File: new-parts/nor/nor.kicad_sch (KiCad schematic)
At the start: 35 parts, among them J1 BHR-10-VUA, J2 BHR-10-VUA, J3 BHR-10-VUA, K1 J104D2C12VDC.15S, K2 J104D2C12VDC.15S, K3 J104D2C12VDC.15S, K4 J104D2C12VDC.15S, K5 J104D2C12VDC.15S, K6 J104D2C12VDC.15S, K7 J104D2C12VDC.15S, K8 J104D2C12VDC.15S

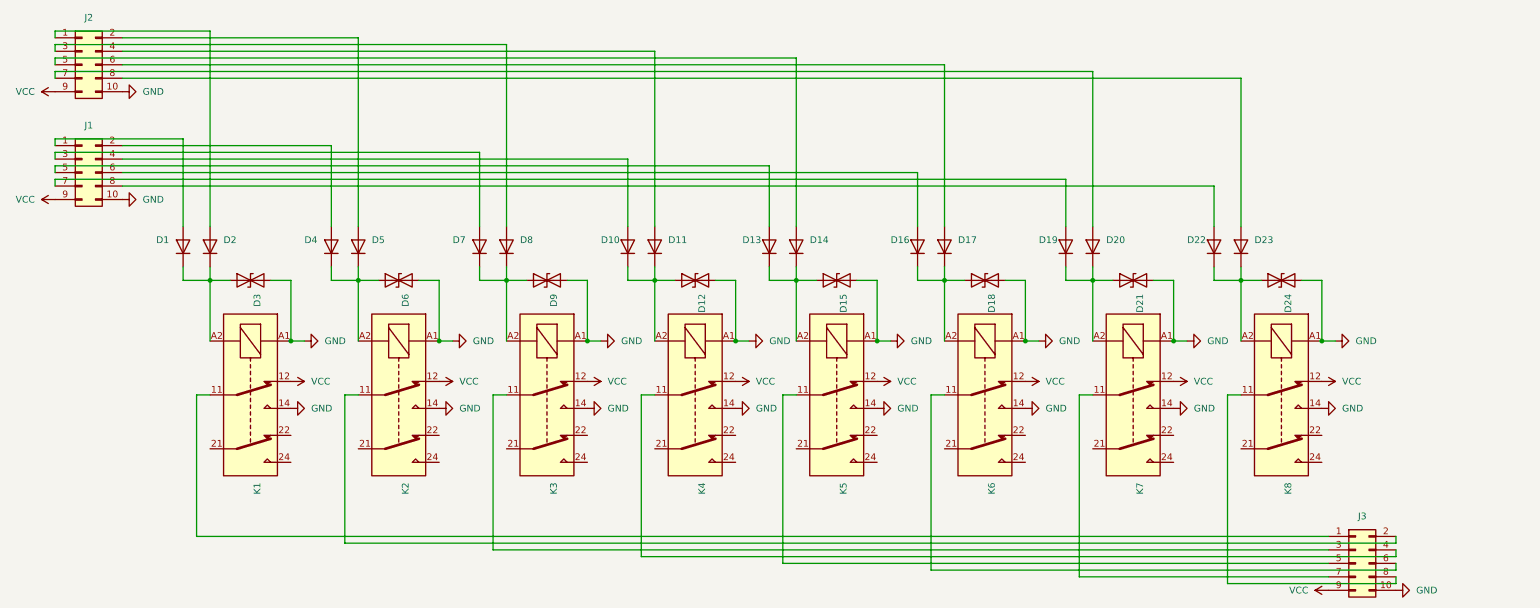
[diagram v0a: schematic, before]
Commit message: Perform BOM export (changes some project settings).
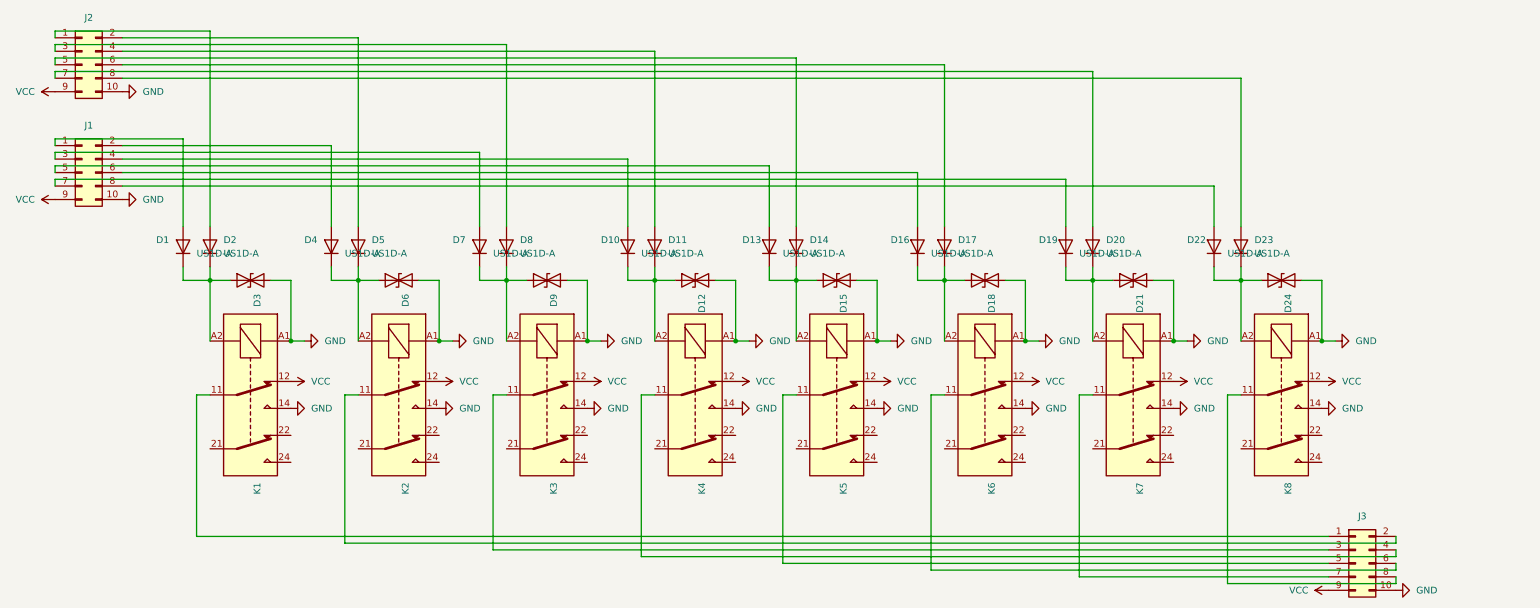
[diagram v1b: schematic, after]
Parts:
- D1, D10, D11, D13, D14, D16, D17, D19, D2, D20, D22, D23, D4, D5, D7, D8: value ~ -> US1D-A
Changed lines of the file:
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@@
 			)
 		)
-		(property "Value" "~"
+		(property "Value" "US1D-A"
 			(at 191.77 69.85 90)
 			(effects
@@
 			)
 		)
-		(property "Datasheet" "~"
+		(property "Datasheet" "https://mm.digikey.com/Volume0/opasdata/d220001/medias/docus/5561/US1A-A%20thru%20US1M-A.pdf"
 			(at 189.23 68.58 0)
 			(effects
@@
 			)
 		)
-		(property "Value" "~"
+		(property "Value" "US1D-A"
 			(at 168.91 69.85 90)
 			(effects
@@
 			)
 		)
-		(property "Datasheet" "~"
+		(property "Datasheet" "https://mm.digikey.com/Volume0/opasdata/d220001/medias/docus/5561/US1A-A%20thru%20US1M-A.pdf"
 			(at 166.37 68.58 0)
 			(effects
@@
 			)
 		)
-		(property "Value" "~"
+		(property "Value" "US1D-A"
 			(at 252.73 69.85 90)
 			(effects
@@
 			)
 		)
-		(property "Datasheet" "~"
+		(property "Datasheet" "https://mm.digikey.com/Volume0/opasdata/d220001/medias/docus/5561/US1A-A%20thru%20US1M-A.pdf"
 			(at 250.19 68.58 0)
 			(effects
@@
 			)
 		)
-		(property "Value" "~"
+		(property "Value" "US1D-A"
 			(at 247.65 69.85 90)
 			(effects
@@
 			)
 		)
-		(property "Datasheet" "~"
+		(property "Datasheet" "https://mm.digikey.com/Volume0/opasdata/d220001/medias/docus/5561/US1A-A%20thru%20US1M-A.pdf"
 			(at 245.11 68.58 0)
 			(effects
@@
 			)
 		)
-		(property "Value" "~"
+		(property "Value" "US1D-A"
 			(at 142.24 69.85 90)
 			(effects
@@
 			)
 		)
-		(property "Datasheet" "~"
+		(property "Datasheet" "https://mm.digikey.com/Volume0/opasdata/d220001/medias/docus/5561/US1A-A%20thru%20US1M-A.pdf"
 			(at 139.7 68.58 0)
 			(effects
@@
 			)
 		)
-		(property "Value" "~"
+		(property "Value" "US1D-A"
 			(at 53.34 69.85 90)
 			(effects
@@
 			)
 		)
-		(property "Datasheet" "~"
+		(property "Datasheet" "https://mm.digikey.com/Volume0/opasdata/d220001/medias/docus/5561/US1A-A%20thru%20US1M-A.pdf"
 			(at 50.8 68.58 0)
 			(effects
@@
 			)
 		)
-		(property "Value" "~"
+		(property "Value" "US1D-A"
 			(at 137.16 69.85 90)
 			(effects
@@
 			)
 		)
-		(property "Datasheet" "~"
+		(property "Datasheet" "https://mm.digikey.com/Volume0/opasdata/d220001/medias/docus/5561/US1A-A%20thru%20US1M-A.pdf"
 			(at 134.62 68.58 0)
 			(effects
@@
 			)
 		)
-		(property "Value" "~"
+		(property "Value" "US1D-A"
 			(at 109.22 69.85 90)
 			(effects
@@
 			)
 		)
-		(property "Datasheet" "~"
+		(property "Datasheet" "https://mm.digikey.com/Volume0/opasdata/d220001/medias/docus/5561/US1A-A%20thru%20US1M-A.pdf"
 			(at 106.68 68.58 0)
 			(effects
@@
 			)
 		)
-		(property "Value" "~"
+		(property "Value" "US1D-A"
 			(at 163.83 69.85 90)
 			(effects
@@
 			)
 		)
-		(property "Datasheet" "~"
+		(property "Datasheet" "https://mm.digikey.com/Volume0/opasdata/d220001/medias/docus/5561/US1A-A%20thru%20US1M-A.pdf"
 			(at 161.29 68.58 0)
 			(effects
@@
 			)
 		)
-		(property "Value" "~"
+		(property "Value" "US1D-A"
 			(at 86.36 69.85 90)
 			(effects
@@
 			)
 		)
-		(property "Datasheet" "~"
+		(property "Datasheet" "https://mm.digikey.com/Volume0/opasdata/d220001/medias/docus/5561/US1A-A%20thru%20US1M-A.pdf"
 			(at 83.82 68.58 0)
 			(effects
@@
 			)
 		)
-		(property "Value" "~"
+		(property "Value" "US1D-A"
 			(at 224.79 69.85 90)
 			(effects
@@
 			)
 		)
-		(property "Datasheet" "~"
+		(property "Datasheet" "https://mm.digikey.com/Volume0/opasdata/d220001/medias/docus/5561/US1A-A%20thru%20US1M-A.pdf"
 			(at 222.25 68.58 0)
 			(effects
@@
 			)
 		)
-		(property "Value" "~"
+		(property "Value" "US1D-A"
 			(at 58.42 69.85 90)
 			(effects
@@
 			)
 		)
-		(property "Datasheet" "~"
+		(property "Datasheet" "https://mm.digikey.com/Volume0/opasdata/d220001/medias/docus/5561/US1A-A%20thru%20US1M-A.pdf"
 			(at 55.88 68.58 0)
 			(effects
@@
 			)
 		)
-		(property "Value" "~"
+		(property "Value" "US1D-A"
 			(at 114.3 69.85 90)
 			(effects
@@
 			)
 		)
-		(property "Datasheet" "~"
+		(property "Datasheet" "https://mm.digikey.com/Volume0/opasdata/d220001/medias/docus/5561/US1A-A%20thru%20US1M-A.pdf"
 			(at 111.76 68.58 0)
 			(effects
@@
 			)
 		)
-		(property "Value" "~"
+		(property "Value" "US1D-A"
 			(at 196.85 69.85 90)
 			(effects
@@
 			)
 		)
-		(property "Datasheet" "~"
+		(property "Datasheet" "https://mm.digikey.com/Volume0/opasdata/d220001/medias/docus/5561/US1A-A%20thru%20US1M-A.pdf"
 			(at 194.31 68.58 0)
 			(effects
@@
 			)
 		)
-		(property "Value" "~"
+		(property "Value" "US1D-A"
 			(at 219.71 69.85 90)
 			(effects
@@
 			)
 		)
-		(property "Datasheet" "~"
+		(property "Datasheet" "https://mm.digikey.com/Volume0/opasdata/d220001/medias/docus/5561/US1A-A%20thru%20US1M-A.pdf"
 			(at 217.17 68.58 0)
 			(effects
@@
 			)
 		)
-		(property "Value" "~"
+		(property "Value" "US1D-A"
 			(at 81.28 69.85 90)
 			(effects
@@
 			)
 		)
-		(property "Datasheet" "~"
+		(property "Datasheet" "https://mm.digikey.com/Volume0/opasdata/d220001/medias/docus/5561/US1A-A%20thru%20US1M-A.pdf"
 			(at 78.74 68.58 0)
 			(effects

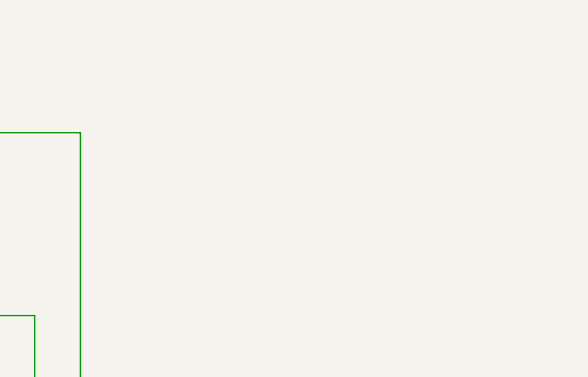
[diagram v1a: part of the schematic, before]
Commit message: Add power connector to nor gate for better GND distribution.
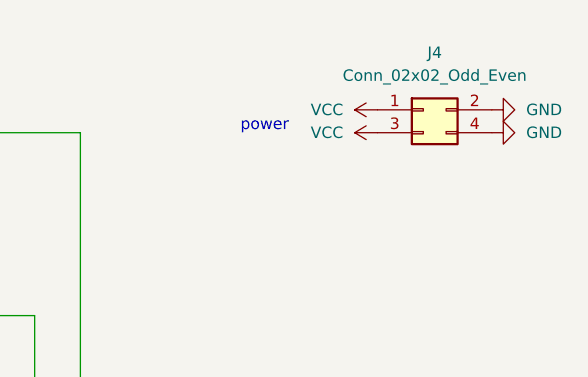
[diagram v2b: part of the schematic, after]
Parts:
- added J4: Conn_02x02_Odd_Even, Connector_PinHeader_2.54mm:PinHeader_2x02_P2.54mm_Vertical, symbol Connector_Generic:Conn_02x02_Odd_Even
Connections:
- net GND: now also J4.2 (Pin_2), J4.4 (Pin_4)
- net VCC: now also J4.1 (Pin_1), J4.3 (Pin_3)
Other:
- note added: "power"
